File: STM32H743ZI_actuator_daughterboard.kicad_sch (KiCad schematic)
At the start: 14 parts, among them J18 Conn_01x02, U1 DAC80508, U3 OPA197xDBV, U5 REF5030AD

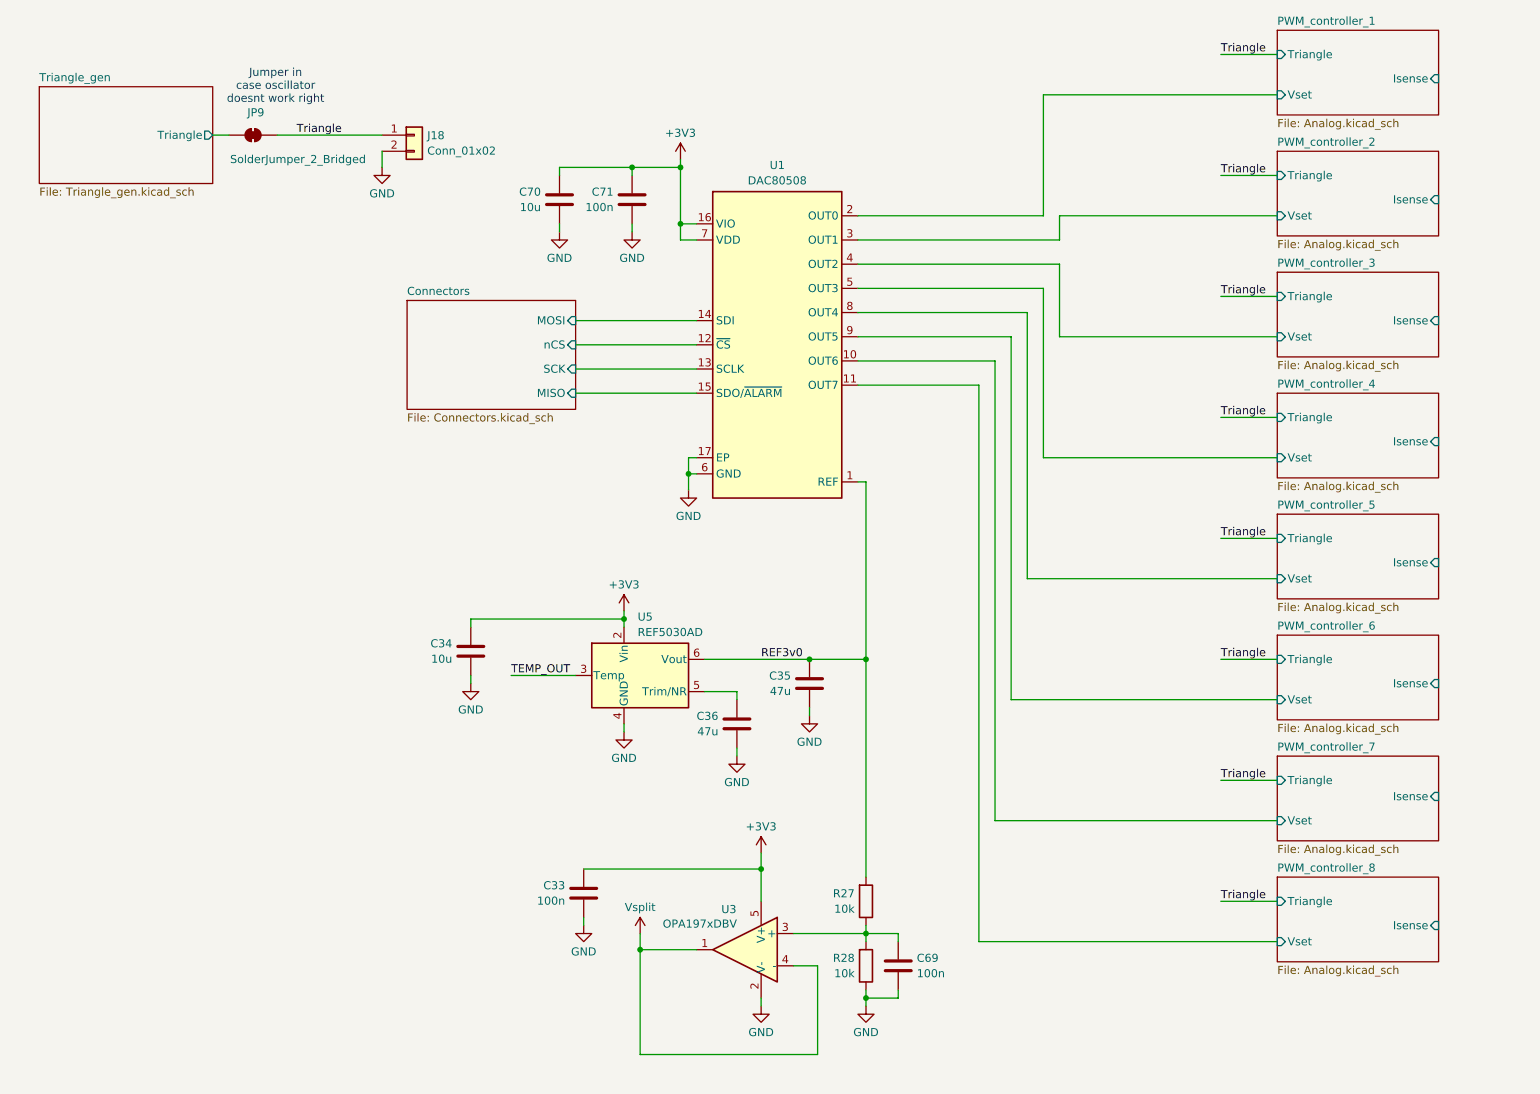
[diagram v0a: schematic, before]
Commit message: 8ch layout applied, connectors aligned to nucleo
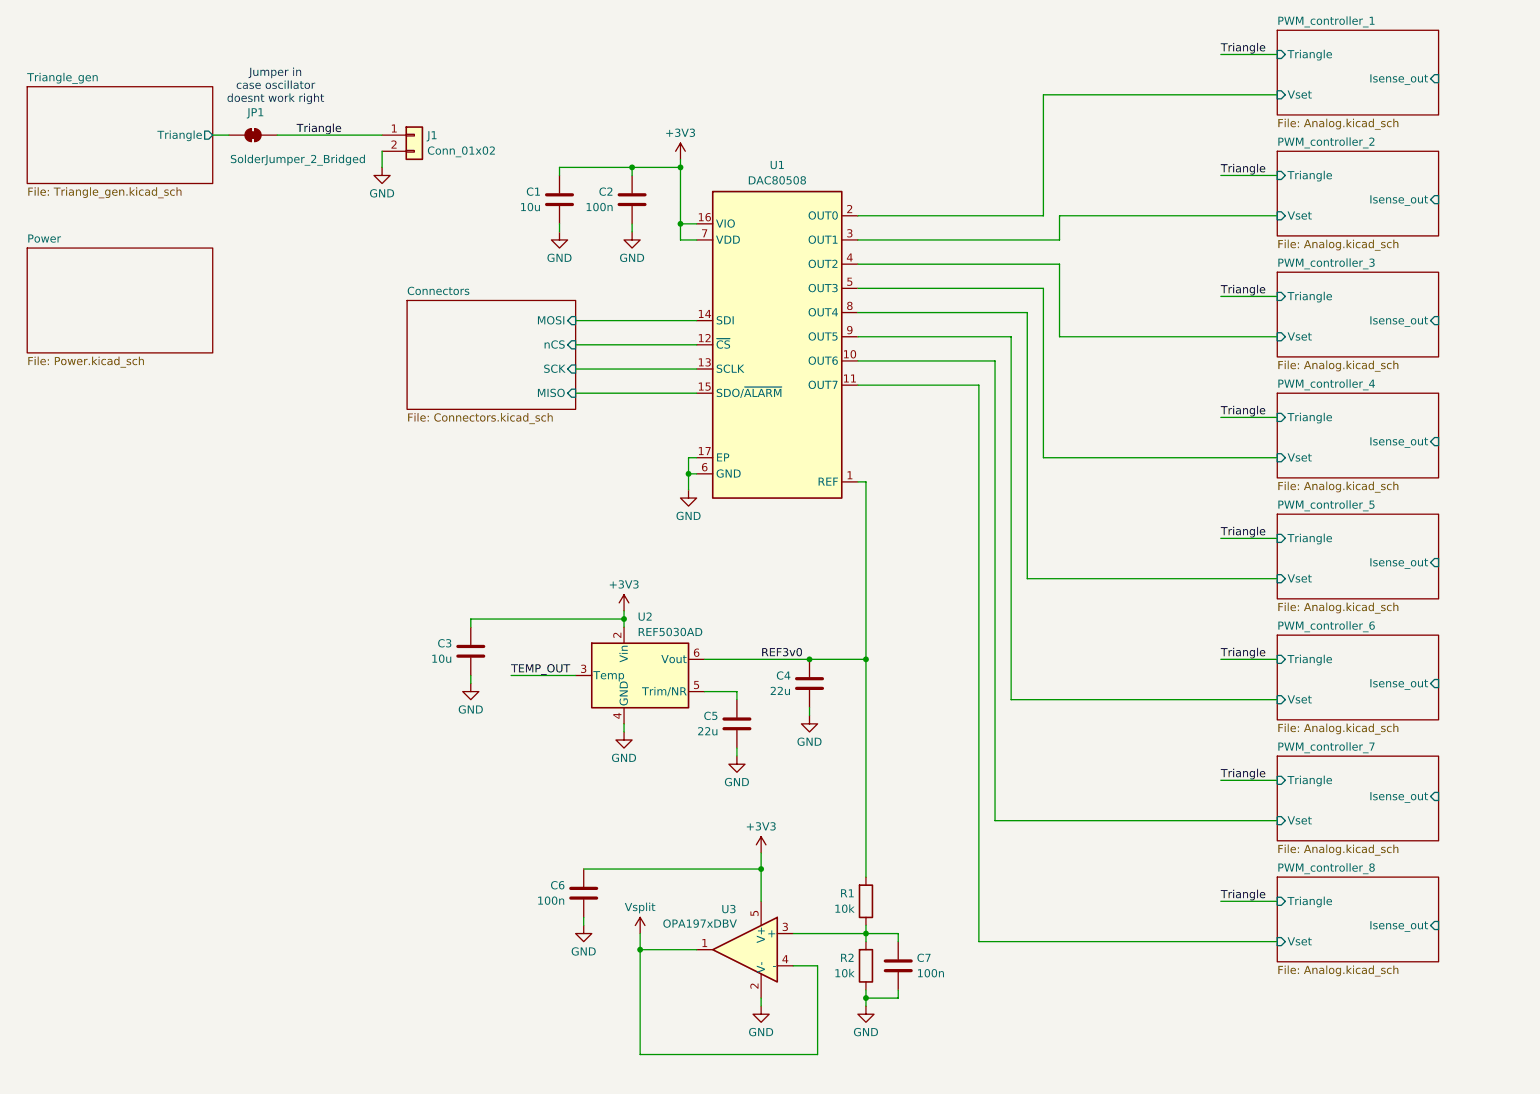
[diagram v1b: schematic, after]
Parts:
- C1: renamed from C70; footprint Capacitor_SMD:C_0805_2012Metric -> Capacitor_SMD:C_0603_1608Metric; LCSC C15850 -> C19702
- C2: renamed from C71; footprint Capacitor_SMD:C_0805_2012Metric -> Capacitor_SMD:C_0603_1608Metric; LCSC C28233 -> C14663
- C3: renamed from C34; footprint Capacitor_SMD:C_0805_2012Metric -> Capacitor_SMD:C_0603_1608Metric; LCSC C15850 -> C19702
- C4: renamed from C35; value 47u -> 22u; footprint Capacitor_SMD:C_0805_2012Metric -> Capacitor_SMD:C_0603_1608Metric; LCSC C16780 -> C59461
- C5: renamed from C36; value 47u -> 22u; footprint Capacitor_SMD:C_0805_2012Metric -> Capacitor_SMD:C_0603_1608Metric; LCSC C16780 -> C59461
- C6: renamed from C33; footprint Capacitor_SMD:C_0805_2012Metric -> Capacitor_SMD:C_0603_1608Metric; LCSC C28233 -> C14663
- C7: renamed from C69; footprint Capacitor_SMD:C_0805_2012Metric -> Capacitor_SMD:C_0603_1608Metric; LCSC C28233 -> C14663
- JP1: renamed from JP9; footprint (none) -> Jumper:SolderJumper-2_P1.3mm_Bridged2Bar_Pad1.0x1.5mm
- R1: renamed from R27; footprint Resistor_SMD:R_0805_2012Metric -> Resistor_SMD:R_0603_1608Metric; LCSC C17414 -> C25804
- R2: renamed from R28; footprint Resistor_SMD:R_0805_2012Metric -> Resistor_SMD:R_0603_1608Metric; LCSC C17414 -> C25804
- renumbered J18 to J1, U5 to U2
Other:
- added sheet Power (Power.kicad_sch)
- sheet PWM_controller_1 ports: added Isense_out; removed Isense
- sheet PWM_controller_2 ports: added Isense_out; removed Isense
- sheet PWM_controller_3 ports: added Isense_out; removed Isense
- sheet PWM_controller_4 ports: added Isense_out; removed Isense
- sheet PWM_controller_5 ports: added Isense_out; removed Isense
- sheet PWM_controller_6 ports: added Isense_out; removed Isense
- sheet PWM_controller_7 ports: added Isense_out; removed Isense
- sheet PWM_controller_8 ports: added Isense_out; removed Isense

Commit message: Working on how to arrange 8 channels
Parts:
- added C69, C70: 1u, Capacitor_SMD:C_0603_1608Metric, symbol Device:C
- added U38: XC6206PxxxMR, Package_TO_SOT_SMD:SOT-23-3, symbol Regulator_Linear:XC6206PxxxMR
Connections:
- net +3V3: now also C70.1, U38.2 (VO)
- net GND: now also C69.2, C70.2, U38.1 (GND)
- new net +5V: C69.1, U38.3 (VI)
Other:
- removed sheet Power
- moved on the sheet: J1, JP1

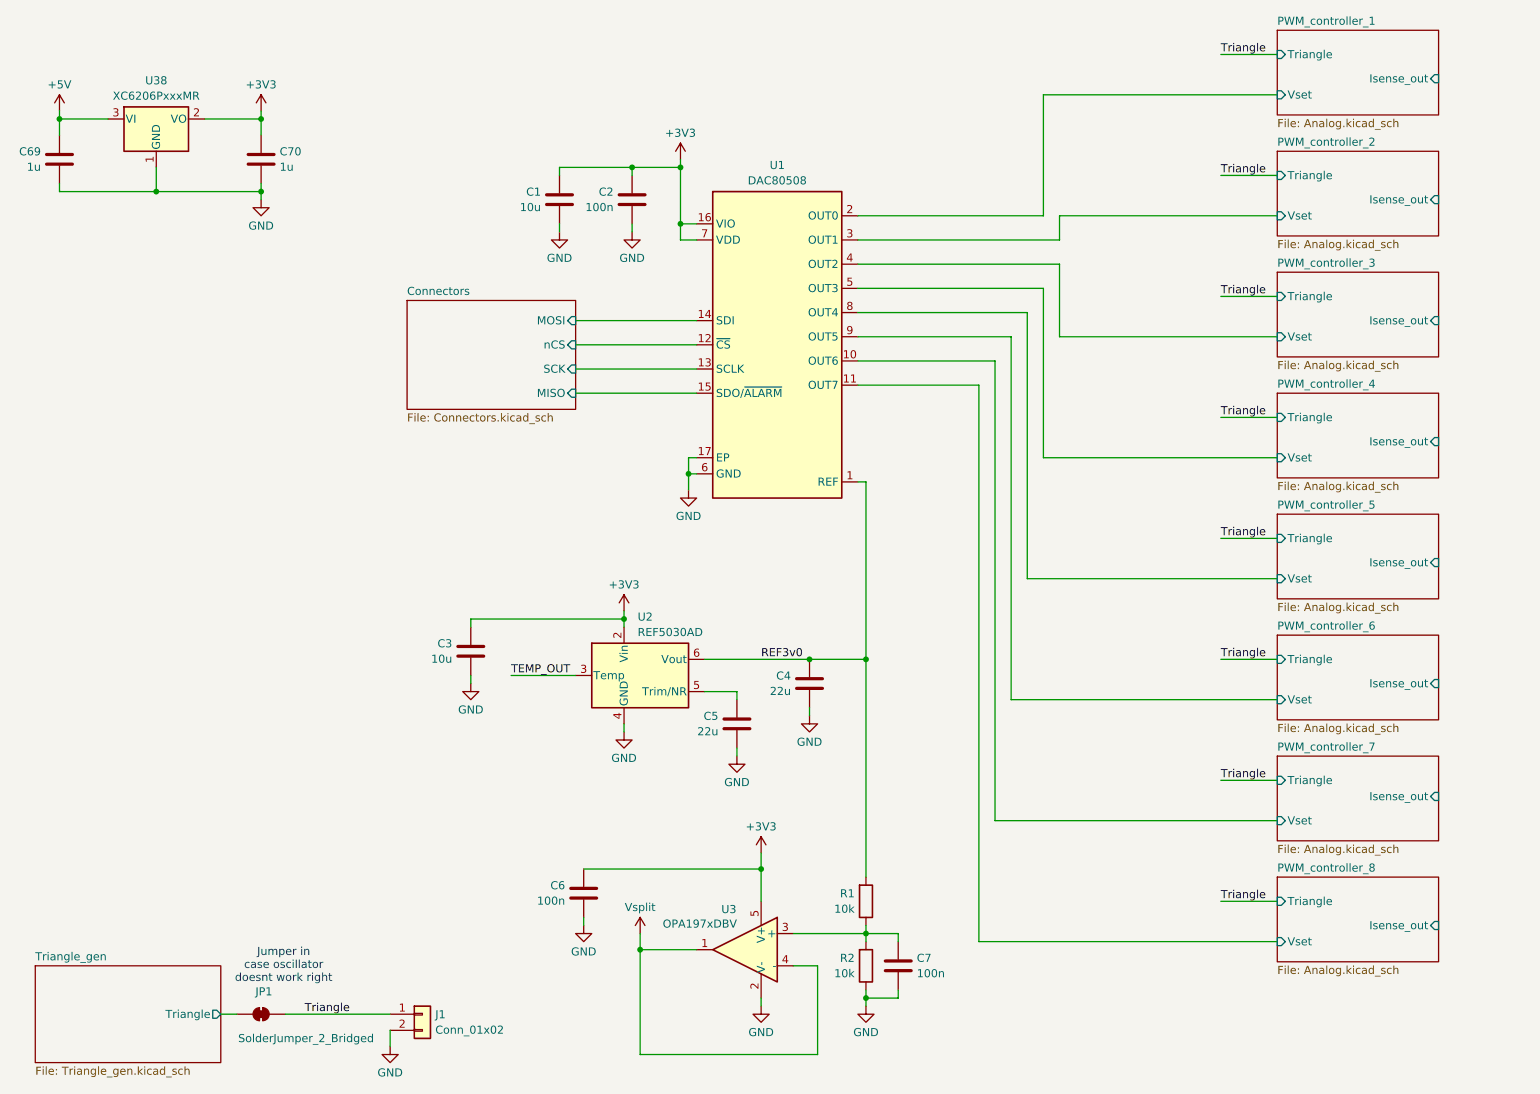
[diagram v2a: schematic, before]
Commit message: Continuing layout, added ADC connections for current measurements
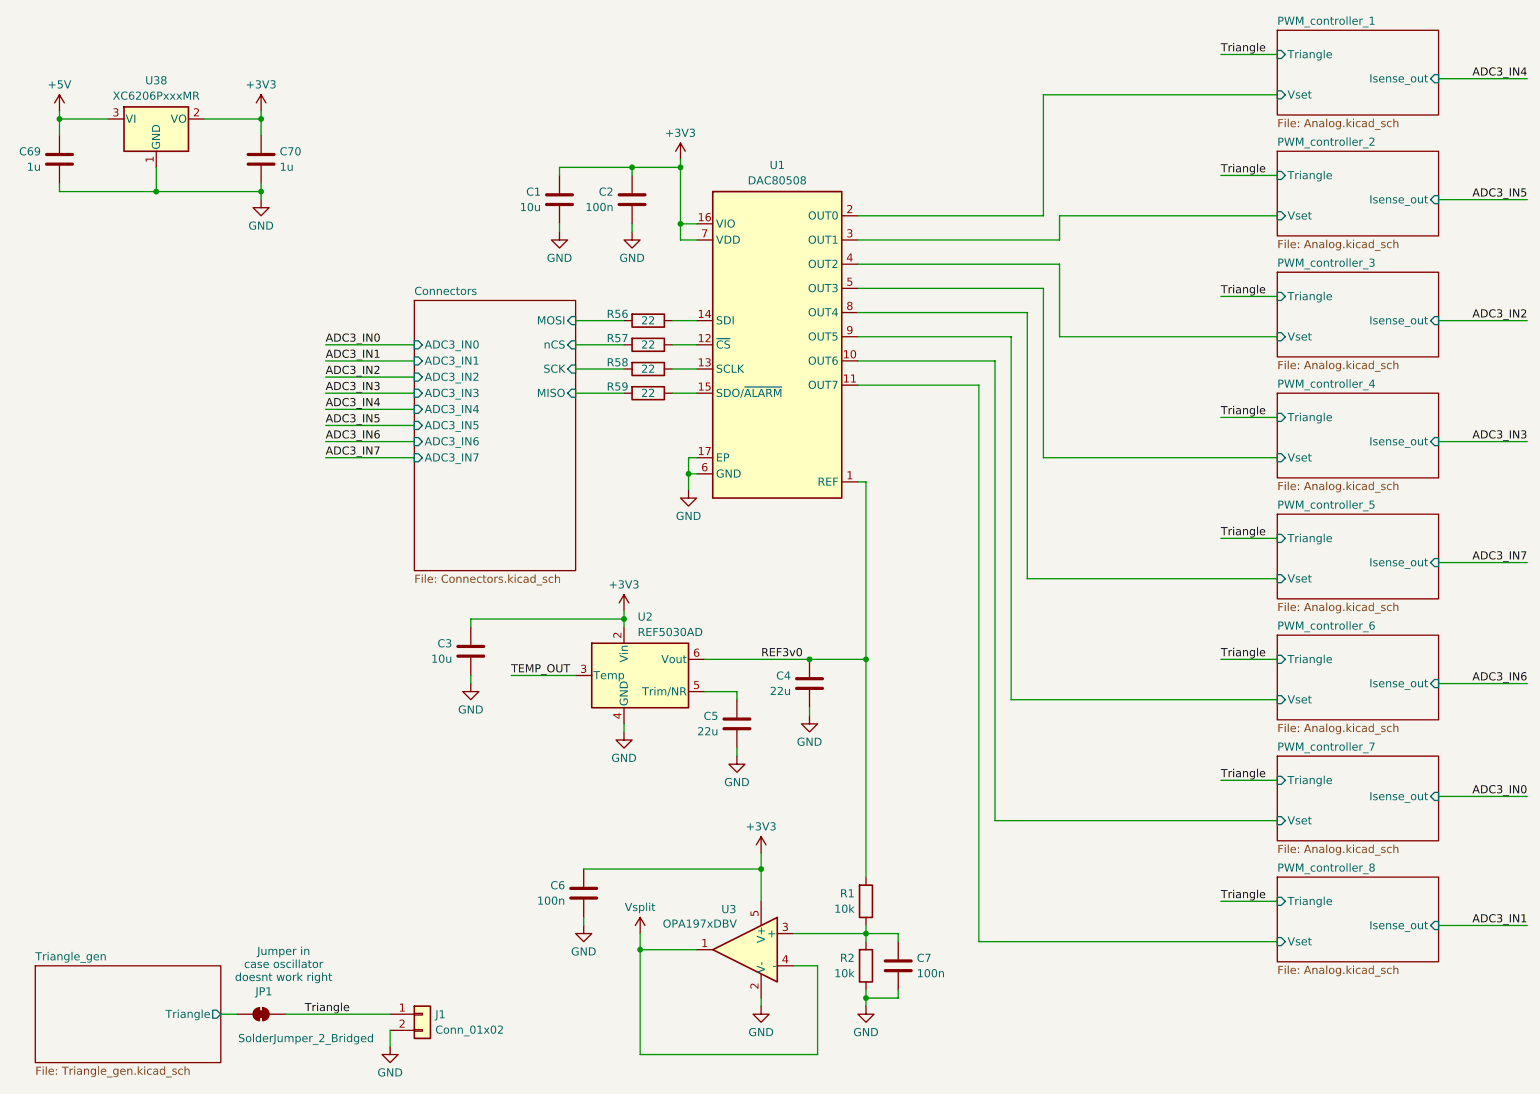
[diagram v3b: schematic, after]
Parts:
- added R56, R57, R58, R59: 22, Resistor_SMD:R_0603_1608Metric, symbol Device:R
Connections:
- net Connectors/MISO: now also R59.2; no longer U1.15 (SDO/~{ALARM})
- net Connectors/MOSI: now also R56.2; no longer U1.14 (SDI)
- net Connectors/SCK: now also R58.2; no longer U1.13 (SCLK)
- net Connectors/nCS: now also R57.2; no longer U1.12 (~{CS})
- new net: R57.1, U1.12 (~{CS})
- new net: R58.1, U1.13 (SCLK)
- new net: R56.1, U1.14 (SDI)
- new net: R59.1, U1.15 (SDO/~{ALARM})
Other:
- sheet Connectors ports: added ADC3_IN0, ADC3_IN1, ADC3_IN2, ADC3_IN3, ADC3_IN4, ADC3_IN5, ADC3_IN6, ADC3_IN7; removed none

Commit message: Basically Done with Layout, final checks and let it sit a day before ordering
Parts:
- added C79: 100n, Capacitor_SMD:C_0603_1608Metric, symbol Device:C
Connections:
- net +3V3: now also C79.1
- net GND: now also C79.2
- net TEMP_OUT: no longer names the net of U2.3 (Temp)
- no-connect marks 0 -> 1
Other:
- moved on the sheet: C1, C2
